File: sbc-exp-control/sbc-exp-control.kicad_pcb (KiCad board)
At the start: 2 copper layers, 76.2 x 24.1 mm, 14 parts, among them J1 P, M1 M2.5, M2 M2.5, M3 M2.5, M4 M2.5, SW1 U, SW2 D, SW3 L, SW4 R, SW5 A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

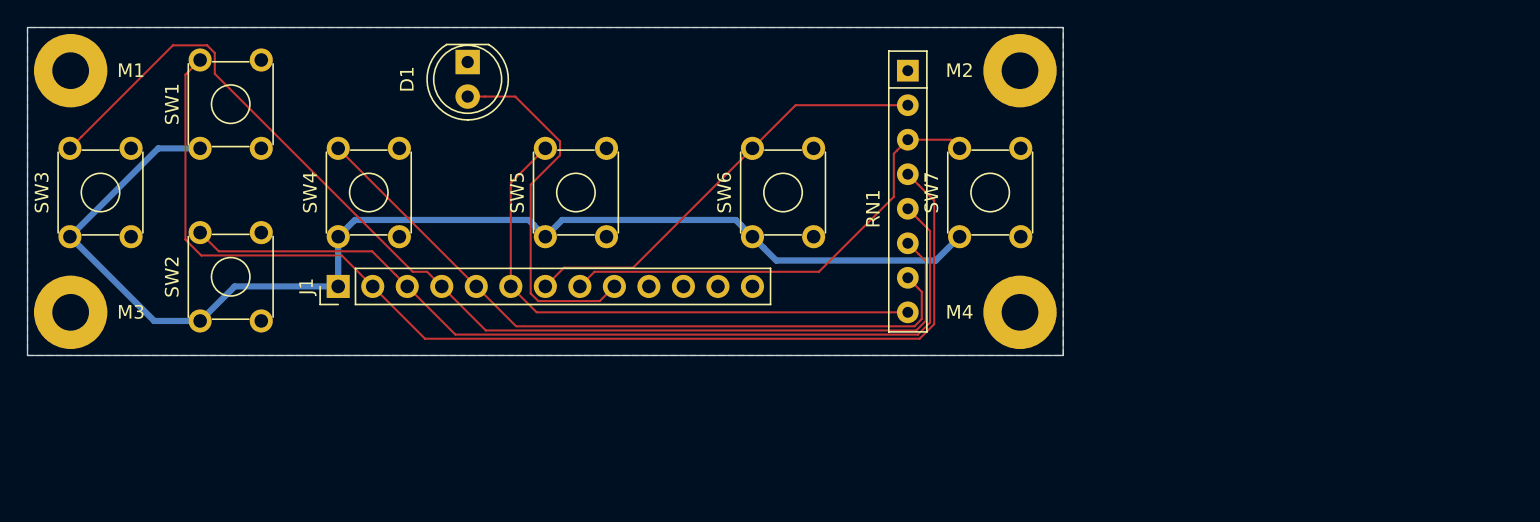
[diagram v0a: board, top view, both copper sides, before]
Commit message: SBC Controller: Fix v1.0 errata
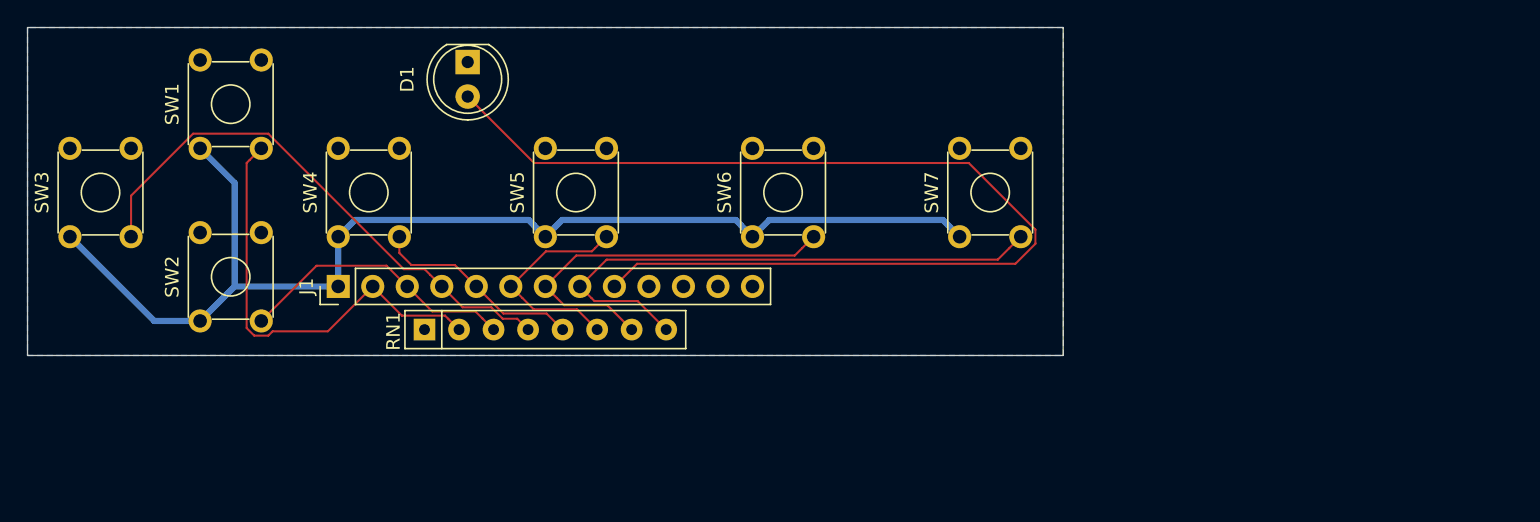
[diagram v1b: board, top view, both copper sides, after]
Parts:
- removed M1, M2, M3, M4: M2.5, mount:MountingHole_2.7mm_M2.5_Pad
- SW1: value U -> UP
- SW2: value D -> DOWN
- SW3: value L -> LEFT
- SW4: value R -> RIGHT
- moved RN1 40.3 mm to (102.9, 89.5), turned to 0 degrees
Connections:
- RN1 pad 2: Net-(J1-Pad7) -> Net-(J1-Pad2)
- RN1 pad 3: Net-(J1-Pad8) -> Net-(J1-Pad3)
- RN1 pad 4: Net-(J1-Pad2) -> Net-(J1-Pad4)
- RN1 pad 5: Net-(J1-Pad3) -> Net-(J1-Pad5)
- RN1 pad 6: Net-(J1-Pad4) -> Net-(J1-Pad6)
- RN1 pad 7: Net-(J1-Pad5) -> Net-(J1-Pad7)
- RN1 pad 8: Net-(J1-Pad6) -> Net-(J1-Pad8)
- SW1 pad 2: Net-(J1-Pad2) -> (no net)
- SW1 pad 3: (no net) -> Net-(J1-Pad2)
- SW2 pad 2: Net-(J1-Pad3) -> (no net)
- SW2 pad 3: (no net) -> Net-(J1-Pad3)
- SW3 pad 2: Net-(J1-Pad4) -> (no net)
- SW3 pad 3: (no net) -> Net-(J1-Pad4)
- SW4 pad 2: Net-(J1-Pad5) -> (no net)
- SW4 pad 3: (no net) -> Net-(J1-Pad5)
- SW5 pad 2: Net-(J1-Pad6) -> (no net)
- SW5 pad 3: (no net) -> Net-(J1-Pad6)
- SW6 pad 2: Net-(J1-Pad7) -> (no net)
- SW6 pad 3: (no net) -> Net-(J1-Pad7)
- SW7 pad 2: Net-(J1-Pad8) -> (no net)
- SW7 pad 3: (no net) -> Net-(J1-Pad8)
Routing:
- net Net-(D1-Pad2): track 27.1 -> 79.1 mm
- net Net-(J1-Pad2): track 84.1 -> 32.3 mm
- net Net-(J1-Pad3): track 66.2 -> 20.7 mm
- net Net-(J1-Pad4): track 82.3 -> 40.1 mm
- net Net-(J1-Pad5): track 52.0 -> 15.5 mm
- net Net-(J1-Pad6): track 41.2 -> 16.2 mm
- net Net-(J1-Pad8): track 34.5 -> 41.6 mm
- net Net-(J1-Pad7): track 32.2 -> 28.9 mm
- net +5V: track 88.5 -> 87.0 mm
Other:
- board text added: "v1.1 © 2021 Daniel Picken https://github.com/dpicken/6502-hw"
- board text removed: "v1.0 © 2021 Daniel Picken https://github.com/dpicken/6502-hw"

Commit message: SBC v2.0
Changes:

 - Second VIA
 - NMI button (hardware debounced)
 - 5 status LEDs (power and each VIA port)
 - Ground and power planes
 - Smaller footprint RAM and oscillator
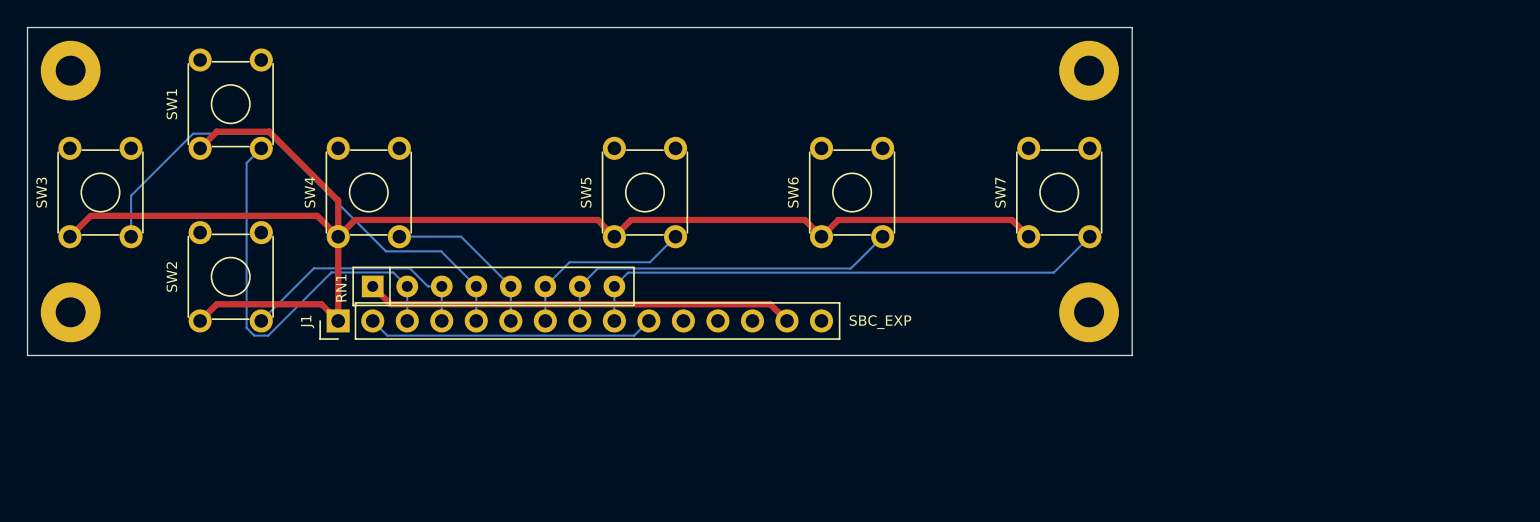
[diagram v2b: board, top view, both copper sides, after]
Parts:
- removed D1: LED, led:LED_D5.0mm
- added M1: M2, mount:MountingHole_2.2mm_M2_Pad, F.Cu at (76.8, 70.5)
- added M2: M2, mount:MountingHole_2.2mm_M2_Pad, F.Cu at (76.8, 88.3)
- added M3: M2, mount:MountingHole_2.2mm_M2_Pad, F.Cu at (151.8, 88.3)
- added M4: M2, mount:MountingHole_2.2mm_M2_Pad, F.Cu at (151.8, 70.5)
- J1: value P -> SBC_EXP; footprint connector:PinHeader_1x13_P2.54mm_Vertical -> connector:PinHeader_1x15_P2.54mm_Vertical
- moved SW6 5.08 mm to (132.1, 82.7)
- moved SW5 5.08 mm to (116.8, 82.7)
- moved SW7 5.08 mm to (147.3, 82.7)
- moved RN1 4.96 mm to (99.1, 86.4)
- moved J1 2.54 mm to (96.5, 88.9)
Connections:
- J1 pad 10: (no net) -> Net-(J1-Pad10)
- J1 pad 11: (no net) -> Net-(J1-Pad11)
- J1 pad 12: (no net) -> Net-(J1-Pad12)
- J1 pad 13: GND -> Net-(J1-Pad13)
- J1 pad 2: Net-(J1-Pad2) -> Net-(J1-Pad10)
- J1 pad 9: Net-(D1-Pad2) -> Net-(J1-Pad9)
- RN1 pad 2: Net-(J1-Pad2) -> Net-(J1-Pad3)
- RN1 pad 3: Net-(J1-Pad3) -> Net-(J1-Pad4)
- RN1 pad 4: Net-(J1-Pad4) -> Net-(J1-Pad5)
- RN1 pad 5: Net-(J1-Pad5) -> Net-(J1-Pad6)
- RN1 pad 6: Net-(J1-Pad6) -> Net-(J1-Pad7)
- RN1 pad 7: Net-(J1-Pad7) -> Net-(J1-Pad8)
- RN1 pad 8: Net-(J1-Pad8) -> Net-(J1-Pad9)
- SW1 pad 3: Net-(J1-Pad2) -> Net-(J1-Pad3)
- SW2 pad 3: Net-(J1-Pad3) -> Net-(J1-Pad4)
- SW3 pad 3: Net-(J1-Pad4) -> Net-(J1-Pad5)
- SW4 pad 3: Net-(J1-Pad5) -> Net-(J1-Pad6)
- SW5 pad 3: Net-(J1-Pad6) -> Net-(J1-Pad7)
- SW6 pad 3: Net-(J1-Pad7) -> Net-(J1-Pad8)
- SW7 pad 3: Net-(J1-Pad8) -> Net-(J1-Pad9)
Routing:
- net Net-(D1-Pad2): track 79.1 -> 0.00 mm
- net Net-(J1-Pad9): track 0.00 -> 39.0 mm
- net Net-(J1-Pad2): track 32.3 -> 0.00 mm
- net GND: track 0.00 -> 31.5 mm
- net Net-(J1-Pad4): track 40.1 -> 18.0 mm
- net Net-(J1-Pad5): track 15.5 -> 37.5 mm
- net Net-(J1-Pad10): track 0.00 -> 21.2 mm
- net +5V: track 87.0 -> 107.7 mm
- net Net-(J1-Pad8): track 41.6 -> 26.3 mm
- net Net-(J1-Pad7): track 28.9 -> 13.6 mm
- net Net-(J1-Pad3): track 20.7 -> 30.6 mm
- net Net-(J1-Pad6): track 16.2 -> 12.3 mm
- removed copper zone on B.Cu, net GND
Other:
- board size 76.2 x 24.1 mm -> 81.3 x 24.1 mm
- board text added: "v2.0 © 2021 Daniel Picken https://github.com/dpicken/6502-hw"
- board text removed: "v1.1 © 2021 Daniel Picken https://github.com/dpicken/6502-hw"

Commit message: SBC v2.2
Changes over v2:

  - Address space decode and IRQ glue logic moved into a PLD
  - Adds serial port and power via USB-C connector
  - Adds onboard microSD mass storage
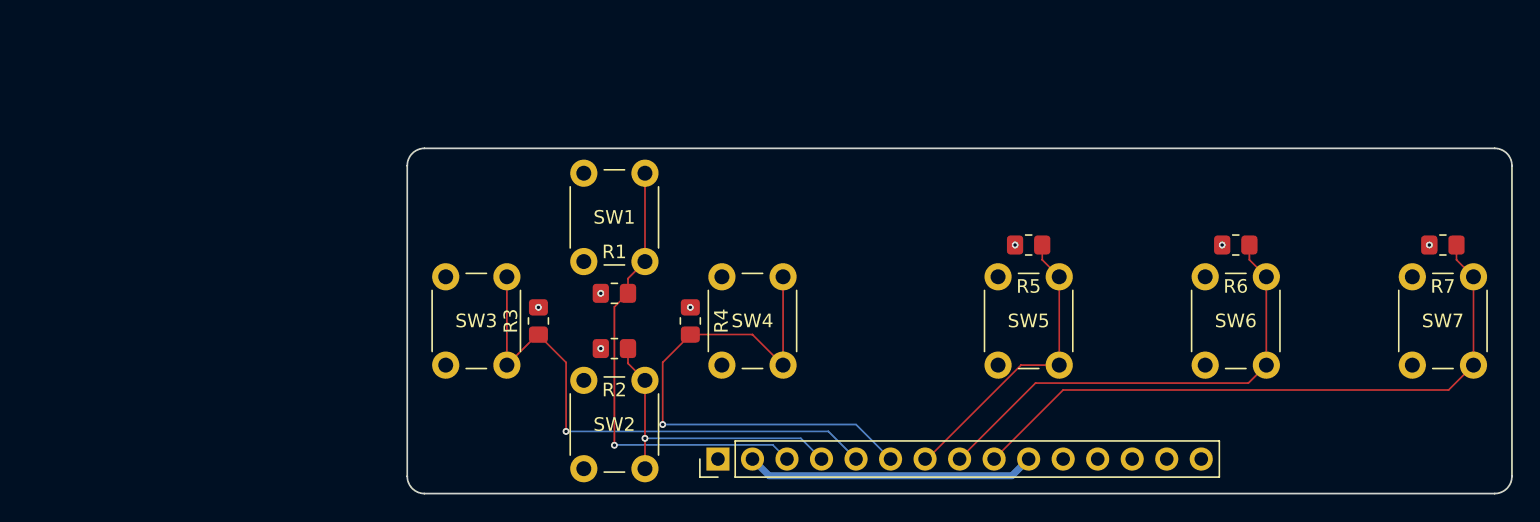
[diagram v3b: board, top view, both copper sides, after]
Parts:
- removed M1, M2, M3, M4: M2, mount:MountingHole_2.2mm_M2_Pad
- removed RN1: 1K, resistor:R_Array_SIP8
- added R1: 1K, Resistor_SMD:R_0805_2012Metric_Pad1.20x1.40mm_HandSolder, F.Cu at (116.8, 86.9)
- added R2: 1K, Resistor_SMD:R_0805_2012Metric_Pad1.20x1.40mm_HandSolder, F.Cu at (116.8, 90.9)
- added R3: 1K, Resistor_SMD:R_0805_2012Metric_Pad1.20x1.40mm_HandSolder, F.Cu at (111.3, 88.9)
- added R4: 1K, Resistor_SMD:R_0805_2012Metric_Pad1.20x1.40mm_HandSolder, F.Cu at (122.4, 88.9)
- added R5: 1K, Resistor_SMD:R_0805_2012Metric_Pad1.20x1.40mm_HandSolder, F.Cu at (147.3, 83.3)
- added R6: 1K, Resistor_SMD:R_0805_2012Metric_Pad1.20x1.40mm_HandSolder, F.Cu at (162.6, 83.3)
- added R7: 1K, Resistor_SMD:R_0805_2012Metric_Pad1.20x1.40mm_HandSolder, F.Cu at (177.8, 83.3)
- J1: footprint connector:PinHeader_1x15_P2.54mm_Vertical -> Connector_PinHeader_2.54mm:PinHeader_1x15_P2.54mm_Vertical
- SW1: value UP -> SW_Push; footprint switch:SW_TH_Tactile_Omron_B3F-10xx -> Button_Switch_THT:SW_PUSH_6mm
- SW2: value DOWN -> SW_Push; footprint switch:SW_TH_Tactile_Omron_B3F-10xx -> Button_Switch_THT:SW_PUSH_6mm
- SW3: value LEFT -> SW_Push; footprint switch:SW_TH_Tactile_Omron_B3F-10xx -> Button_Switch_THT:SW_PUSH_6mm
- SW4: value RIGHT -> SW_Push; footprint switch:SW_TH_Tactile_Omron_B3F-10xx -> Button_Switch_THT:SW_PUSH_6mm
- SW5: value A -> SW_Push; footprint switch:SW_TH_Tactile_Omron_B3F-10xx -> Button_Switch_THT:SW_PUSH_6mm
- SW6: value B -> SW_Push; footprint switch:SW_TH_Tactile_Omron_B3F-10xx -> Button_Switch_THT:SW_PUSH_6mm
- SW7: value C -> SW_Push; footprint switch:SW_TH_Tactile_Omron_B3F-10xx -> Button_Switch_THT:SW_PUSH_6mm
- moved SW2 30.3 mm to (114.6, 99.8)
- moved SW7 29.8 mm to (175.6, 92.2)
- moved SW4 29.8 mm to (124.8, 92.2)
- moved SW5 29.8 mm to (145.1, 92.2)
- moved SW6 29.8 mm to (160.3, 92.2)
- moved J1 29.7 mm to (124.5, 99.1)
- moved SW1 29.4 mm to (114.6, 84.5)
- moved SW3 29.2 mm to (104.4, 92.2)
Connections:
- net Net-(J1-Pad10) renamed LED_ENABLE
- J1 pad 11: Net-(J1-Pad11) -> unconnected-(J1-Pad11)
- J1 pad 12: Net-(J1-Pad12) -> unconnected-(J1-Pad12)
- J1 pad 13: Net-(J1-Pad13) -> unconnected-(J1-Pad13)
- J1 pad 15: Net-(J1-Pad15) -> unconnected-(J1-Pad15)
- J1 pad 3: Net-(J1-Pad3) -> UP
- J1 pad 4: Net-(J1-Pad4) -> DOWN
- J1 pad 5: Net-(J1-Pad5) -> LEFT
- J1 pad 6: Net-(J1-Pad6) -> RIGHT
- J1 pad 7: Net-(J1-Pad7) -> A
- J1 pad 8: Net-(J1-Pad8) -> B
- J1 pad 9: Net-(J1-Pad9) -> C
- SW1 pad 2: (no net) -> UP
- SW2 pad 2: (no net) -> DOWN
- SW3 pad 2: (no net) -> LEFT
- SW4 pad 2: (no net) -> RIGHT
- SW5 pad 2: (no net) -> A
- SW6 pad 2: (no net) -> B
- SW7 pad 2: (no net) -> C
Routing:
- net +5V: track 107.7 -> 0.00 mm
- net C: track 0.00 -> 47.5 mm
- net LEFT: track 0.00 -> 39.9 mm, vias 0 -> 1
- net RIGHT: track 0.00 -> 39.5 mm, vias 0 -> 1
- net Net-(J1-Pad9): track 39.0 -> 0.00 mm
- net Net-(J1-Pad5): track 37.5 -> 0.00 mm
- net B: track 0.00 -> 34.8 mm
- net UP: track 0.00 -> 34.1 mm, vias 0 -> 1
- net GND: track 31.5 -> 0.00 mm, vias 0 -> 7
- net Net-(J1-Pad3): track 30.6 -> 0.00 mm
- net Net-(J1-Pad8): track 26.3 -> 0.00 mm
- net DOWN: track 0.00 -> 22.7 mm, vias 0 -> 1
- net A: track 0.00 -> 22.1 mm
- net Net-(J1-Pad4): track 18.0 -> 0.00 mm
- net Net-(J1-Pad7): track 13.6 -> 0.00 mm
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- added copper zone on In2.Cu, net +5V
- added copper zone on In1.Cu, net GND
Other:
- board size 81.3 x 24.1 mm -> 81.3 x 25.4 mm
- copper layers 2 -> 4
- net class Default removed
- net class Power removed
- rule pad_to_mask_clearance: 0.0508 -> 0
- board text added: "v2.2 | © 2022 Daniel Picken | https://github.com/dpicken/6502-hw"
- board text removed: "v2.0 © 2021 Daniel Picken https://github.com/dpicken/6502-hw"

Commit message: SBC v2.3
Fixes over v2.2:

  - SBC: Fix the VIA footprint: CA1 and CB1 are inputs
  - SBC: Move the microSD power enable line from (VIA3) CA1 (input) to CA2 (output)
  - Controller: connect LED enable
  - Controller: SMT switches
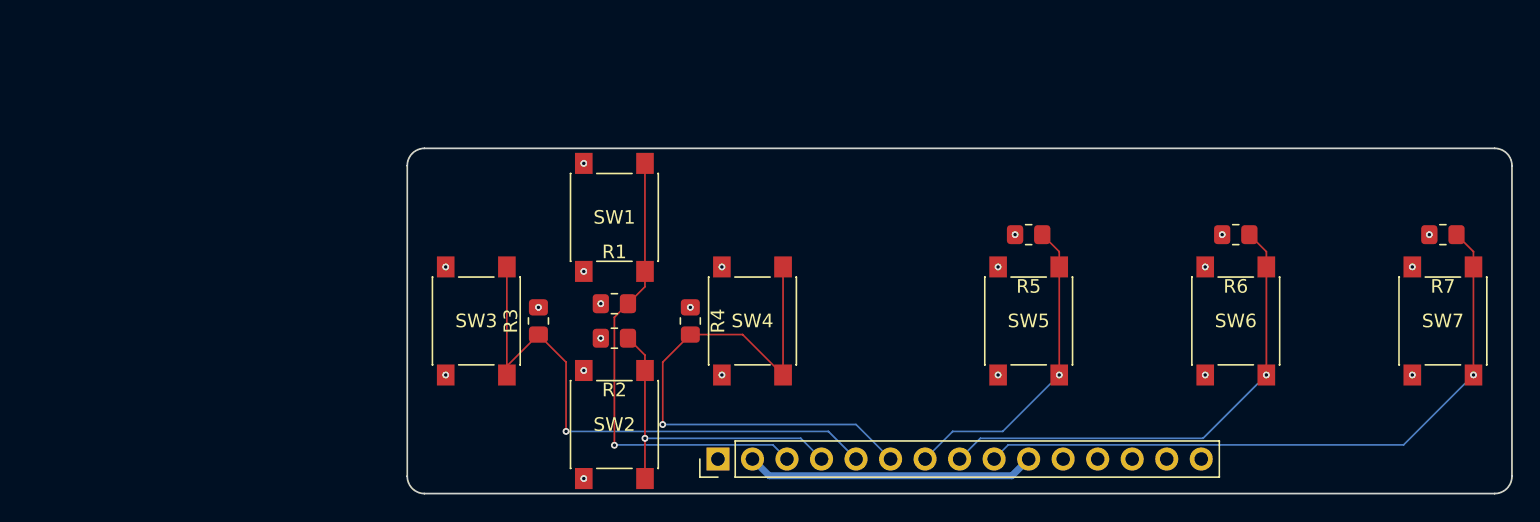
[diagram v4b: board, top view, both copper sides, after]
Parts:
- SW1, SW2, SW3, SW4, SW5, SW6, SW7: footprint Button_Switch_THT:SW_PUSH_6mm -> Button_Switch_SMD:SW_Push_1P1T_NO_6x6mm_H9.5mm
- moved SW1 3.95 mm to (116.8, 81.3)
- moved SW2 3.95 mm to (116.8, 96.5)
- moved SW3 3.95 mm to (106.7, 88.9)
- moved SW4 3.95 mm to (127.0, 88.9)
- moved SW5 3.95 mm to (147.3, 88.9)
- moved SW6 3.95 mm to (162.6, 88.9)
- moved SW7 3.95 mm to (177.8, 88.9)
- moved R1 0.76 mm to (116.8, 87.6)
- moved R2 0.76 mm to (116.8, 90.2)
- moved R5 0.76 mm to (147.3, 82.5)
- moved R6 0.76 mm to (162.6, 82.5)
- moved R7 0.76 mm to (177.8, 82.5)
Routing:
- net LEFT: track 39.9 -> 42.0 mm
- net RIGHT: track 39.5 -> 41.3 mm
- net DOWN: track 22.7 -> 24.2 mm
- net C: track 47.5 -> 48.7 mm, vias 0 -> 1
- net B: track 34.8 -> 36.0 mm, vias 0 -> 1
- net A: track 22.1 -> 23.3 mm, vias 0 -> 1
- net UP: track 34.1 -> 34.8 mm
- net +5V: vias 0 -> 14
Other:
- board text added: "v2.3 | © 2022 Daniel Picken | https://github.com/dpicken/6502-hw"
- board text removed: "v2.2 | © 2022 Daniel Picken | https://github.com/dpicken/6502-hw"
